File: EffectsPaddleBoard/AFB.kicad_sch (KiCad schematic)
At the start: 22 parts, among them J5 AudioJack2, J6 AudioJack2, U5 MCP6401T-xLT, U6 MCP6401T-xLT, U7 MCP6401T-xLT

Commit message: Began with pcb layout
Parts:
- added H1, H2, H3, H4: MountingHole, MountingHole:MountingHole_3.2mm_M3, symbol Mechanical:MountingHole
- C29: footprint (none) -> Capacitor_SMD:C_0402_1005Metric
- C29: footprint (none) -> Capacitor_SMD:C_1206_3216Metric
- C29: footprint (none) -> Capacitor_SMD:C_1210_3225Metric
- C29: value 10u -> 220p; footprint (none) -> Capacitor_SMD:C_0402_1005Metric
- J5, J6: footprint (none) -> Connector_Audio:Jack_6.35mm_Neutrik_NJ2FD-V_Vertical
- R13, R21, R22: footprint (none) -> Resistor_SMD:R_0402_1005Metric
- RV1: footprint (none) -> Potentiometer_THT:Potentiometer_Bourns_3005_Horizontal
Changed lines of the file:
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@@
       (effects (font (size 1.27 1.27)) (justify right))
     )
-    (property "Footprint" "" (at 94.615 67.945 0)
+    (property "Footprint" "Resistor_SMD:R_0402_1005Metric" (at 94.615 67.945 0)
       (effects (font (size 1.27 1.27)) hide)
     )
@@
     )
   )
+  (symbol (lib_id "Mechanical:MountingHole") (at 248.92 26.67 0) (unit 1)
+    (in_bom yes) (on_board yes) (dnp no) (fields_autoplaced)
+    (property "Reference" "H2" (at 251.46 26.035 0)
+      (effects (font (size 1.27 1.27)) (justify left))
+    )
+    (property "Value" "MountingHole" (at 251.46 28.575 0)
+      (effects (font (size 1.27 1.27)) (justify left))
+    )
+    (property "Footprint" "MountingHole:MountingHole_3.2mm_M3" (at 248.92 26.67 0)
+      (effects (font (size 1.27 1.27)) hide)
+    )
+    (property "Datasheet" "~" (at 248.92 26.67 0)
+      (effects (font (size 1.27 1.27)) hide)
+    )
+    (instances
+      (project "EffectsPaddleBoard"
+        (path "/40bb1606-5207-4492-95b9-876879aab2b4/ff9bb951-f2c7-47aa-9bab-7296304b78b4"
+          (reference "H2") (unit 1)
+        )
+      )
+    )
+  )
   (symbol (lib_id "Device:C_Small") (at 125.73 118.11 90) (unit 1)
     (in_bom yes) (on_board yes) (dnp no) (fields_autoplaced)
@@
       (effects (font (size 1.27 1.27)))
     )
-    (property "Footprint" "" (at 125.73 118.11 0)
+    (property "Footprint" "Capacitor_SMD:C_0402_1005Metric" (at 125.73 118.11 0)
       (effects (font (size 1.27 1.27)) hide)
     )
@@
       (effects (font (size 1.27 1.27)))
     )
-    (property "Footprint" "" (at 66.04 60.325 0)
+    (property "Footprint" "Resistor_SMD:R_0402_1005Metric" (at 66.04 60.325 0)
       (effects (font (size 1.27 1.27)) hide)
     )
@@
       (effects (font (size 1.27 1.27)))
     )
-    (property "Footprint" "" (at 156.21 62.865 0)
+    (property "Footprint" "Capacitor_SMD:C_1206_3216Metric" (at 156.21 62.865 0)
       (effects (font (size 1.27 1.27)) hide)
     )
@@
       (effects (font (size 1.27 1.27)))
     )
-    (property "Footprint" "" (at 151.765 133.985 0)
+    (property "Footprint" "Resistor_SMD:R_0402_1005Metric" (at 151.765 133.985 0)
       (effects (font (size 1.27 1.27)) hide)
     )
@@
       (effects (font (size 1.27 1.27)) (justify right))
     )
-    (property "Footprint" "" (at 94.615 52.07 0)
+    (property "Footprint" "Resistor_SMD:R_0402_1005Metric" (at 94.615 52.07 0)
       (effects (font (size 1.27 1.27)) hide)
     )
@@
     )
   )
+  (symbol (lib_id "Mechanical:MountingHole") (at 226.06 38.735 0) (unit 1)
+    (in_bom yes) (on_board yes) (dnp no) (fields_autoplaced)
+    (property "Reference" "H3" (at 228.6 38.1 0)
+      (effects (font (size 1.27 1.27)) (justify left))
+    )
+    (property "Value" "MountingHole" (at 228.6 40.64 0)
+      (effects (font (size 1.27 1.27)) (justify left))
+    )
+    (property "Footprint" "MountingHole:MountingHole_3.2mm_M3" (at 226.06 38.735 0)
+      (effects (font (size 1.27 1.27)) hide)
+    )
+    (property "Datasheet" "~" (at 226.06 38.735 0)
+      (effects (font (size 1.27 1.27)) hide)
+    )
+    (instances
+      (project "EffectsPaddleBoard"
+        (path "/40bb1606-5207-4492-95b9-876879aab2b4/ff9bb951-f2c7-47aa-9bab-7296304b78b4"
+          (reference "H3") (unit 1)
+        )
+      )
+    )
+  )
   (symbol (lib_id "Device:C_Small") (at 217.805 131.445 90) (unit 1)
     (in_bom yes) (on_board yes) (dnp no) (fields_autoplaced)
@@
       (effects (font (size 1.27 1.27)))
     )
-    (property "Footprint" "" (at 217.805 131.445 0)
+    (property "Footprint" "Capacitor_SMD:C_1210_3225Metric" (at 217.805 131.445 0)
       (effects (font (size 1.27 1.27)) hide)
     )
@@
       (effects (font (size 1.27 1.27)) (justify left))
     )
-    (property "Value" "10u" (at 78.74 69.2213 0)
-      (effects (font (size 1.27 1.27)) (justify left))
-    )
-    (property "Footprint" "" (at 75.565 67.31 0)
+    (property "Value" "220p" (at 78.74 69.2213 0)
+      (effects (font (size 1.27 1.27)) (justify left))
+    )
+    (property "Footprint" "Capacitor_SMD:C_0402_1005Metric" (at 75.565 67.31 0)
       (effects (font (size 1.27 1.27)) hide)
     )
@@
       (effects (font (size 1.27 1.27)) (justify left))
     )
-    (property "Footprint" "" (at 108.585 43.815 0)
+    (property "Footprint" "Capacitor_SMD:C_0402_1005Metric" (at 108.585 43.815 0)
       (effects (font (size 1.27 1.27)) hide)
     )
@@
       (effects (font (size 1.27 1.27)))
     )
-    (property "Footprint" "" (at 121.92 109.855 0)
+    (property "Footprint" "Resistor_SMD:R_0402_1005Metric" (at 121.92 109.855 0)
       (effects (font (size 1.27 1.27)) hide)
     )
@@
       (effects (font (size 1.27 1.27)) (justify right))
     )
-    (property "Footprint" "" (at 201.295 147.32 0)
+    (property "Footprint" "Potentiometer_THT:Potentiometer_Bourns_3005_Horizontal" (at 201.295 147.32 0)
       (effects (font (size 1.27 1.27)) hide)
     )
@@
     )
   )
+  (symbol (lib_id "Mechanical:MountingHole") (at 226.06 26.67 0) (unit 1)
+    (in_bom yes) (on_board yes) (dnp no) (fields_autoplaced)
+    (property "Reference" "H1" (at 228.6 26.035 0)
+      (effects (font (size 1.27 1.27)) (justify left))
+    )
+    (property "Value" "MountingHole" (at 228.6 28.575 0)
+      (effects (font (size 1.27 1.27)) (justify left))
+    )
+    (property "Footprint" "MountingHole:MountingHole_3.2mm_M3" (at 226.06 26.67 0)
+      (effects (font (size 1.27 1.27)) hide)
+    )
+    (property "Datasheet" "~" (at 226.06 26.67 0)
+      (effects (font (size 1.27 1.27)) hide)
+    )
+    (instances
+      (project "EffectsPaddleBoard"
+        (path "/40bb1606-5207-4492-95b9-876879aab2b4/ff9bb951-f2c7-47aa-9bab-7296304b78b4"
+          (reference "H1") (unit 1)
+        )
+      )
+    )
+  )
   (symbol (lib_id "Connector_Audio:AudioJack2") (at 241.3 131.445 180) (unit 1)
     (in_bom yes) (on_board yes) (dnp no) (fields_autoplaced)
@@
       (effects (font (size 1.27 1.27)) (justify right))
     )
-    (property "Footprint" "" (at 241.3 131.445 0)
+    (property "Footprint" "Connector_Audio:Jack_6.35mm_Neutrik_NJ2FD-V_Vertical" (at 241.3 131.445 0)
       (effects (font (size 1.27 1.27)) hide)
     )
@@
       (effects (font (size 1.27 1.27)))
     )
-    (property "Footprint" "" (at 100.965 136.525 0)
+    (property "Footprint" "Resistor_SMD:R_0402_1005Metric" (at 100.965 136.525 0)
       (effects (font (size 1.27 1.27)) hide)
     )
@@
     )
   )
+  (symbol (lib_id "Mechanical:MountingHole") (at 248.92 38.735 0) (unit 1)
+    (in_bom yes) (on_board yes) (dnp no) (fields_autoplaced)
+    (property "Reference" "H4" (at 251.46 38.1 0)
+      (effects (font (size 1.27 1.27)) (justify left))
+    )
+    (property "Value" "MountingHole" (at 251.46 40.64 0)
+      (effects (font (size 1.27 1.27)) (justify left))
+    )
+    (property "Footprint" "MountingHole:MountingHole_3.2mm_M3" (at 248.92 38.735 0)
+      (effects (font (size 1.27 1.27)) hide)
+    )
+    (property "Datasheet" "~" (at 248.92 38.735 0)
+      (effects (font (size 1.27 1.27)) hide)
+    )
+    (instances
+      (project "EffectsPaddleBoard"
+        (path "/40bb1606-5207-4492-95b9-876879aab2b4/ff9bb951-f2c7-47aa-9bab-7296304b78b4"
+          (reference "H4") (unit 1)
+        )
+      )
+    )
+  )
   (symbol (lib_id "power:GND") (at 108.585 49.53 0) (unit 1)
     (in_bom yes) (on_board yes) (dnp no) (fields_autoplaced)
@@
       (effects (font (size 1.27 1.27)) (justify left))
     )
-    (property "Footprint" "" (at 58.42 136.525 0)
+    (property "Footprint" "Resistor_SMD:R_0402_1005Metric" (at 58.42 136.525 0)
       (effects (font (size 1.27 1.27)) hide)
     )
@@
       (effects (font (size 1.27 1.27)))
     )
-    (property "Footprint" "" (at 82.55 60.325 0)
+    (property "Footprint" "Capacitor_SMD:C_0402_1005Metric" (at 82.55 60.325 0)
       (effects (font (size 1.27 1.27)) hide)
     )
@@
       (effects (font (size 1.27 1.27)) (justify right))
     )
-    (property "Footprint" "" (at 170.815 78.105 0)
+    (property "Footprint" "Resistor_SMD:R_0402_1005Metric" (at 170.815 78.105 0)
       (effects (font (size 1.27 1.27)) hide)
     )
@@
       (effects (font (size 1.27 1.27)))
     )
-    (property "Footprint" "" (at 184.15 115.57 0)
+    (property "Footprint" "Capacitor_SMD:C_0402_1005Metric" (at 184.15 115.57 0)
       (effects (font (size 1.27 1.27)) hide)
     )
@@
       (effects (font (size 1.27 1.27)) (justify left))
     )
-    (property "Footprint" "" (at 58.42 126.365 0)
+    (property "Footprint" "Resistor_SMD:R_0402_1005Metric" (at 58.42 126.365 0)
       (effects (font (size 1.27 1.27)) hide)
     )
@@
       (effects (font (size 1.27 1.27)))
     )
-    (property "Footprint" "" (at 47.625 60.325 0)
-      (effects (font (size 1.27 1.27)) hide)
-    )
+    (property "Footprint" "Connector_Audio:Jack_6.35mm_Neutrik_NJ2FD-V_Vertical" (at 47.625 60.325 0)
+      (effects (font (size 1.27 1.27)) hide)
+    )

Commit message: Reviev by David and netnaming
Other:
- note added: "closely look again...seems sus"
- company: (none) -> Selbstständig
- title: (none) -> Effects Paddle
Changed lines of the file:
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@@
 (kicad_sch (version 20230121) (generator eeschema)
   (paper "A4")
+  (title_block
+    (title "Effects Paddle")
+    (date "2023-07-01")
+    (rev "0.1")
+    (company "Selbstständig")
+  )
   (junction (at 144.78 133.985) (diameter 0) (color 0 0 0 0)
   )
@@
     (stroke (width 0) (type default))
   )
+  (text "closely look again...seems sus" (at 199.39 68.58 0)
+    (effects (font (size 1.27 1.27)) (justify left bottom))
+  )
   (text "Audio In" (at 22.86 24.765 0)

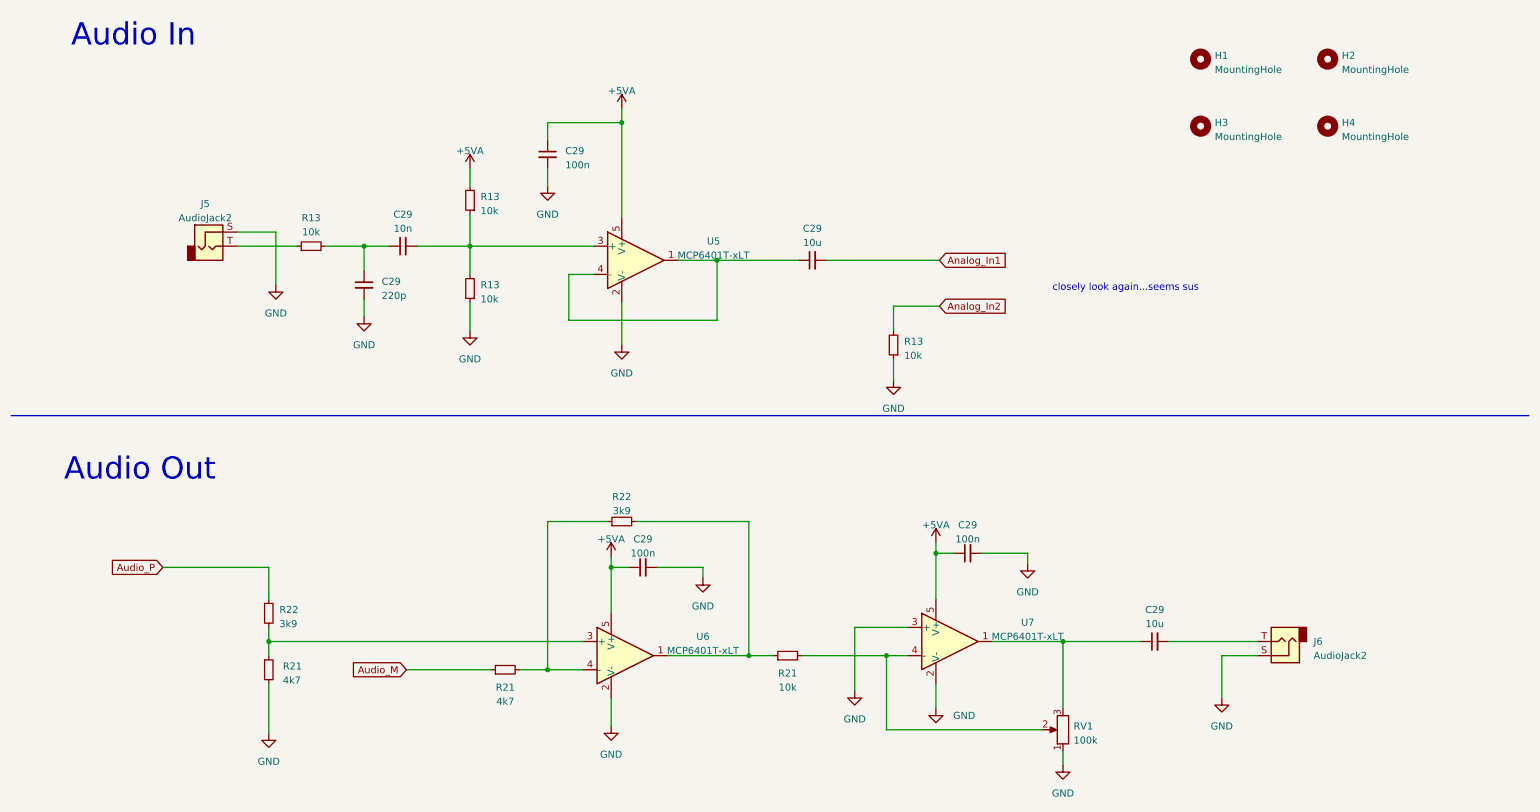
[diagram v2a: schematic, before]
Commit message: Proceeded in layout, just power is missing
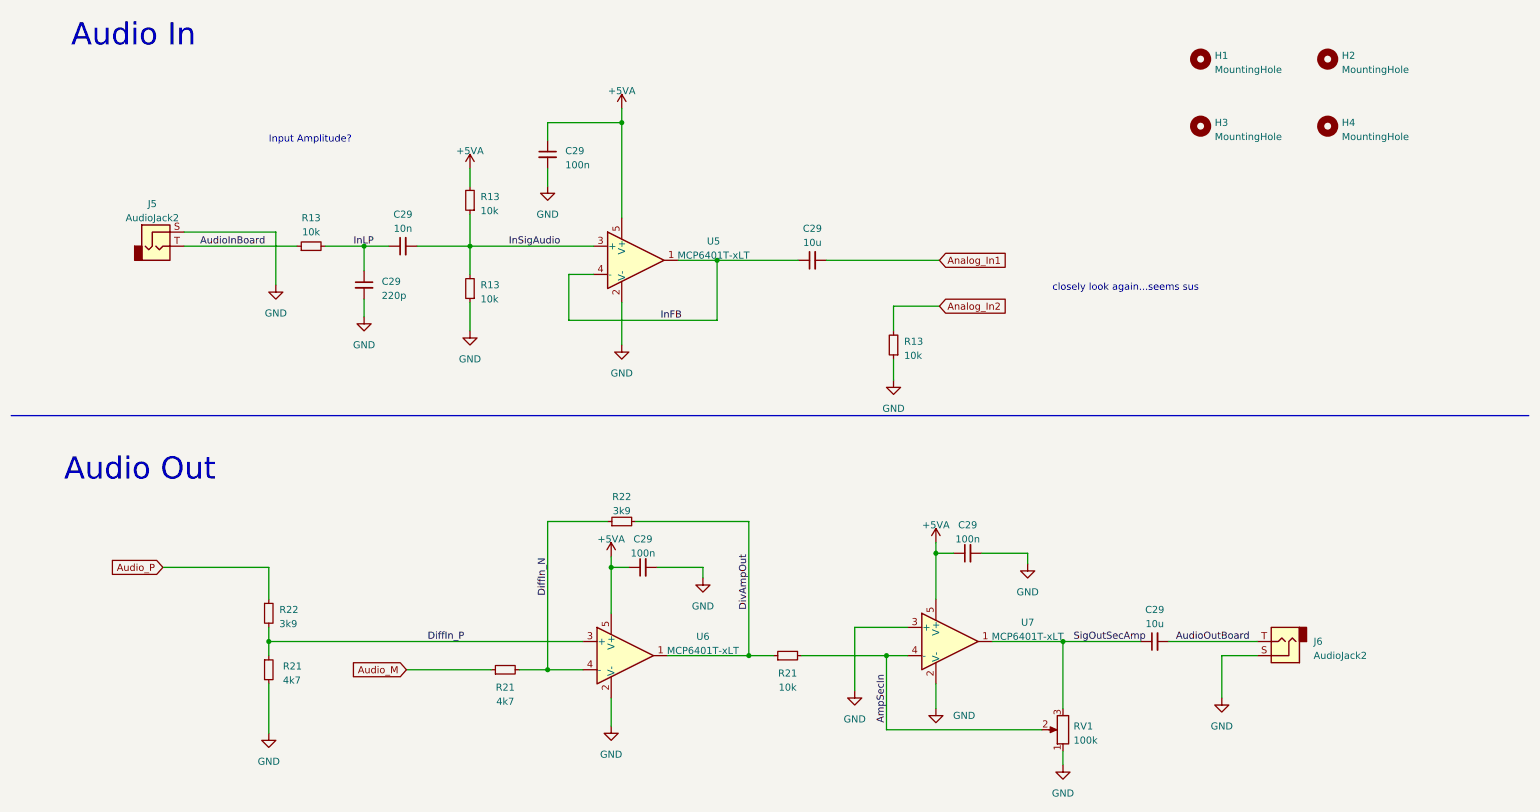
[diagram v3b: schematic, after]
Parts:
- C29: footprint Capacitor_SMD:C_1210_3225Metric -> Capacitor_SMD:C_1206_3216Metric
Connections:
- net InSigAudio: now reaches C29.2, R13.1, R13.2, U5.3 (+)
- net AudioInBoard: now reaches J5.T, R13.1
- net InLP: now reaches C29.1, C29.1, R13.2
- net DivAmpOut: now reaches R21.1, R22.2, U6.1
- net DiffIn_P: now reaches R21.1, R22.2, U6.3 (+)
- net DiffIn_N: now reaches R21.2, R22.1, U6.4 (-)
- net InFB: now reaches C29.1, U5.1, U5.4 (-)
- net AmpSecIn: now reaches R21.2, RV1.2, U7.4 (-)
- net SigOutSecAmp: now reaches C29.1, RV1.3, U7.1
- net AudioOutBoard: now reaches C29.2, J6.T
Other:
- note added: "Input Amplitude?"
- moved on the sheet: J5
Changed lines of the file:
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@@
     (stroke (width 0) (type default))
   )
-  (wire (pts (xy 52.705 60.325) (xy 63.5 60.325))
+  (wire (pts (xy 43.18 60.325) (xy 63.5 60.325))
     (stroke (width 0) (type default))
   )
@@
     (stroke (width 0) (type default))
   )
-  (wire (pts (xy 52.705 57.785) (xy 59.69 57.785))
+  (wire (pts (xy 43.18 57.785) (xy 59.69 57.785))
     (stroke (width 0) (type default))
   )
@@
     (effects (font (size 4 4)) (justify left bottom))
   )
+  (text "Input Amplitude?" (at 58.42 41.91 0)
+    (effects (font (size 1.27 1.27)) (justify left bottom))
+  )
   (text "Audio Out" (at 21.59 102.87 0)
     (effects (font (size 4 4)) (justify left bottom))
+  )
+  (label "DiffIn_P" (at 86.995 131.445 0) (fields_autoplaced)
+    (effects (font (size 1.27 1.27)) (justify left bottom))
+  )
+  (label "AudioOutBoard" (at 221.615 131.445 0) (fields_autoplaced)
+    (effects (font (size 1.27 1.27)) (justify left bottom))
+  )
+  (label "DiffIn_N" (at 108.585 123.19 90) (fields_autoplaced)
+    (effects (font (size 1.27 1.27)) (justify left bottom))
+  )
+  (label "AmpSecIn" (at 169.545 146.05 90) (fields_autoplaced)
+    (effects (font (size 1.27 1.27)) (justify left bottom))
+  )
+  (label "DivAmpOut" (at 144.78 125.73 90) (fields_autoplaced)
+    (effects (font (size 1.27 1.27)) (justify left bottom))
+  )
+  (label "InSigAudio" (at 101.6 60.325 0) (fields_autoplaced)
+    (effects (font (size 1.27 1.27)) (justify left bottom))
+  )
+  (label "InFB" (at 128.905 73.66 0) (fields_autoplaced)
+    (effects (font (size 1.27 1.27)) (justify left bottom))
+  )
+  (label "AudioInBoard" (at 57.785 60.325 180) (fields_autoplaced)
+    (effects (font (size 1.27 1.27)) (justify right bottom))
+  )
+  (label "SigOutSecAmp" (at 203.2 131.445 0) (fields_autoplaced)
+    (effects (font (size 1.27 1.27)) (justify left bottom))
+  )
+  (label "InLP" (at 73.66 60.325 0) (fields_autoplaced)
+    (effects (font (size 1.27 1.27)) (justify left bottom))
   )
   (global_label "Audio_M" (shape input) (at 83.185 136.525 180) (fields_autoplaced)
@@
       (effects (font (size 1.27 1.27)))
     )
-    (property "Footprint" "Capacitor_SMD:C_1210_3225Metric" (at 217.805 131.445 0)
+    (property "Footprint" "Capacitor_SMD:C_1206_3216Metric" (at 217.805 131.445 0)
       (effects (font (size 1.27 1.27)) hide)
     )
@@
     )
   )
-  (symbol (lib_id "Connector_Audio:AudioJack2") (at 47.625 60.325 0) (unit 1)
-    (in_bom yes) (on_board yes) (dnp no) (fields_autoplaced)
-    (property "Reference" "J5" (at 46.99 52.705 0)
-      (effects (font (size 1.27 1.27)))
-    )
-    (property "Value" "AudioJack2" (at 46.99 55.245 0)
-      (effects (font (size 1.27 1.27)))
-    )
-    (property "Footprint" "Connector_Audio:Jack_6.35mm_Neutrik_NJ2FD-V_Vertical" (at 47.625 60.325 0)
-      (effects (font (size 1.27 1.27)) hide)
-    )
-    (property "Datasheet" "~" (at 47.625 60.325 0)
-      (effects (font (size 1.27 1.27)) hide)
-    )
+  (symbol (lib_id "Connector_Audio:AudioJack2") (at 38.1 60.325 0) (unit 1)
+    (in_bom yes) (on_board yes) (dnp no) (fields_autoplaced)
+    (property "Reference" "J5" (at 37.465 52.705 0)
+      (effects (font (size 1.27 1.27)))
+    )
+    (property "Value" "AudioJack2" (at 37.465 55.245 0)
+      (effects (font (size 1.27 1.27)))
+    )
+    (property "Footprint" "Connector_Audio:Jack_6.35mm_Neutrik_NJ2FD-V_Vertical" (at 38.1 60.325 0)
+      (effects (font (size 1.27 1.27)) hide)
+    )
+    (property "Datasheet" "~" (at 38.1 60.325 0)
+      (effects (font (size 1.27 1.27)) hide)
+    )

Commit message: Finished layout
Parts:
- removed C29: 10u, Capacitor_SMD:C_1206_3216Metric, symbol Device:C_Small
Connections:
- net InFB is gone; now on net Analog_In1: U5.1, U5.4 (-)
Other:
- note added: "DC-decoupling at codec page"
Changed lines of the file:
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@@
-    (stroke (width 0) (type default))
-  )
-  (wire (pts (xy 139.065 62.865) (xy 153.67 62.865))
     (stroke (width 0) (type default))
   )
@@
     (stroke (width 0) (type default))
   )
-  (wire (pts (xy 158.75 62.865) (xy 179.07 62.865))
+  (wire (pts (xy 139.065 62.865) (xy 179.07 62.865))
     (stroke (width 0) (type default))
   )
@@
   (text "Audio Out" (at 21.59 102.87 0)
     (effects (font (size 4 4)) (justify left bottom))
+  )
+  (text "DC-decoupling at codec page" (at 153.035 59.69 0)
+    (effects (font (size 1.27 1.27)) (justify left bottom))
   )
   (label "DiffIn_P" (at 86.995 131.445 0) (fields_autoplaced)
@@
         )
       )
-    )
-  )
-  (symbol (lib_id "Device:C_Small") (at 156.21 62.865 90) (unit 1)
-    (in_bom yes) (on_board yes) (dnp no) (fields_autoplaced)
-    (property "Reference" "C29" (at 156.2163 57.15 90)
-      (effects (font (size 1.27 1.27)))
-    )
-    (property "Value" "10u" (at 156.2163 59.69 90)
-      (effects (font (size 1.27 1.27)))
-    )
-    (property "Footprint" "Capacitor_SMD:C_1206_3216Metric" (at 156.21 62.865 0)
-      (effects (font (size 1.27 1.27)) hide)
-    )
-    (property "Datasheet" "~" (at 156.21 62.865 0)
-      (effects (font (size 1.27 1.27)) hide)
-    )
-    (pin "1")
-    (pin "2")
-    (instances
-      (project "EffectsPaddleBoard"
-        (path "/40bb1606-5207-4492-95b9-876879aab2b4"
-          (reference "C29") (unit 1)
-        )
-        (path "/40bb1606-5207-4492-95b9-876879aab2b4/ff9bb951-f2c7-47aa-9bab-7296304b78b4"
-          (reference "C47") (unit 1)
-        )
-      )
